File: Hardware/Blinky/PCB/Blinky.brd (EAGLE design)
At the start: 72.2 x 12 mm, 29 parts, among them Q1 IRLML2502, Q2 IRLML2502, Q3 IRLML2502, U1 ATMEGAU2-AU, U2 MTCH101, U3 TS3USB30EDGSR, X1 USB-A-PCB, X2 USB-A-PCB, Y1 ABM3

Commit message: Changed the series resistance on the USB lines to 16 Ohm.
The USB switch U3 is introducing some additional resistance in the on state.
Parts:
- R1, R2: value 22 -> 16
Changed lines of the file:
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@@
 <element name="C3" library="rcl" package="C0805" value="27p" x="51.25" y="1.5"/>
 <element name="Y1" library="mibe" package="ABM3" value="ABM3" x="51.25" y="6" rot="R90"/>
-<element name="R1" library="rcl" package="R0805" value="22" x="55.25" y="7.25" rot="R180"/>
-<element name="R2" library="rcl" package="R0805" value="22" x="55.25" y="4.75" rot="R180"/>
+<element name="R1" library="rcl" package="R0805" value="16" x="55.25" y="7.25" rot="R180"/>
+<element name="R2" library="rcl" package="R0805" value="16" x="55.25" y="4.75" rot="R180"/>
 <element name="X1" library="mibe" package="USB-A-PCB" value="USB-A-PCB" x="63.6" y="6" rot="MR0"/>
 <element name="X2" library="mibe" package="USB-A-PCB" value="USB-A-PCB" x="63.6" y="6" rot="R180"/>

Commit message: Imported the BISS logo into the Blinky PCB.
This also determined the final size of the PCB.
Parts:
- added U$2: LOGO, BISS:LOGO
- U$1: value BISS-LOGO -> LOGO; device mibe:BISS-LOGO -> BISS:LOGO
- moved U$1 11.8 mm to (0.38, 11.7)
- moved C1 1.88 mm to (45.4, 10.5)
- moved C2 1.88 mm to (49.4, 10.5)
- moved C3 1.88 mm to (49.4, 1.50)
- moved C4 1.88 mm to (53.4, 1.50)
- moved C5 1.88 mm to (45.4, 1.50)
- moved D1 1.88 mm to (58.1, 1.50)
- moved D2 1.88 mm to (58.1, 10.5)
- moved D3 1.88 mm to (35.6, 6.00)
- moved Q1 1.88 mm to (38.0, 9.25)
- moved Q2 1.88 mm to (38.0, 6.00)
- moved Q3 1.88 mm to (38.0, 2.75)
- moved R1 1.88 mm to (53.4, 7.25)
- moved R10 1.88 mm to (32.9, 6.00)
- moved R11 1.88 mm to (32.9, 3.75)
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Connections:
- net TOUCH_PAD: now also U$2.P$1
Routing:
- net TOUCH_PAD: track 16.6 -> 55.2 mm, vias 0 -> 1
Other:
- board size 72.2 x 12 mm -> 70.4 x 12 mm

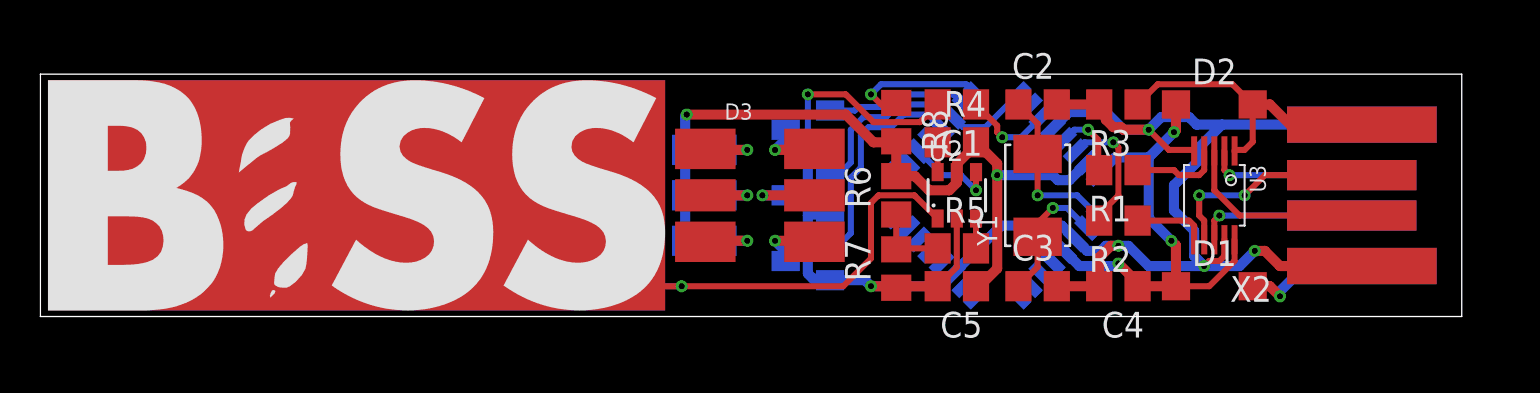
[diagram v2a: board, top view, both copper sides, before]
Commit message: Added ground pour on both sides and moved some traces and vias around.
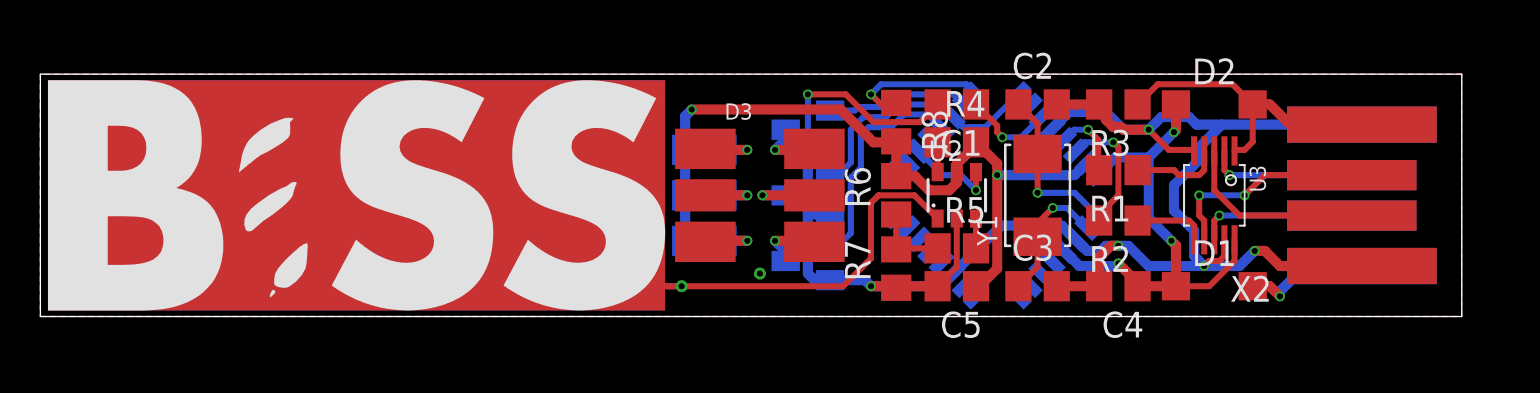
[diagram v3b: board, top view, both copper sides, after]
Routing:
- net GND: vias 6 -> 7
- added copper zone on layer 1, net GND
- added copper zone on layer 16, net GND
